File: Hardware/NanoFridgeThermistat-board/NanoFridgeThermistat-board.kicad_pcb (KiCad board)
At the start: 2 copper layers, 80.5 x 72.1 mm, 63 parts, among them J1 Connector_Thermistor, J2 Main_Connector, J3 CompressorMotor_Connector, J4 I2C_Conn, J5 Connector_Thermistor, SW1 SW_Push, SW2 SW_Push, T1 CST1, U1 MOC3042M, U2 TL072

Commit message: Added mother-daughter boards connector on mother board as well
Signed-off-by: bebenlebricolo <benoittarrade@hotmail.fr>
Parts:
- added J6: Connector_Thermistor, Connector_PinSocket_2.54mm:PinSocket_1x02_P2.54mm_Vertical, F.Cu at (120.4, 115.8)
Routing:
- net GND: track 15.5 -> 17.5 mm, vias 37 -> 36
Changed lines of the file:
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@@
     )
   )
+  (footprint "Connector_PinSocket_2.54mm:PinSocket_1x02_P2.54mm_Vertical" (layer "F.Cu")
+    (at 120.396 115.824)
+    (descr "Through hole straight socket strip, 1x02, 2.54mm pitch, single row (from Kicad 4.0.7), script generated")
+    (tags "Through hole socket strip THT 1x02 2.54mm single row")
+    (property "Sheetfile" "NanoFridgeThermistat-board.kicad_sch")
+    (property "Sheetname" "")
+    (property "ki_description" "Generic connector, single row, 01x02, script generated")
+    (property "ki_keywords" "connector")
+    (attr through_hole)
+    (fp_text reference "J6" (at -0.508 -2.794) (layer "F.SilkS")
+        (effects (font (size 1 1) (thickness 0.15)))
+    )
+    (fp_text value "Connector_Thermistor" (at 0 5.31) (layer "F.Fab")
+        (effects (font (size 1 1) (thickness 0.15)))
+    )
+    (fp_text user "${REFERENCE}" (at 0 1.27 90) (layer "F.Fab")
+        (effects (font (size 1 1) (thickness 0.15)))
+    )
+    (fp_line (start -1.33 1.27) (end -1.33 3.87)
+      (stroke (width 0.12) (type solid)) (layer "F.SilkS"))
+    (fp_line (start -1.33 1.27) (end 1.33 1.27)
+      (stroke (width 0.12) (type solid)) (layer "F.SilkS"))
+    (fp_line (start -1.33 3.87) (end 1.33 3.87)
+      (stroke (width 0.12) (type solid)) (layer "F.SilkS"))
+    (fp_line (start 0 -1.33) (end 1.33 -1.33)
+      (stroke (width 0.12) (type solid)) (layer "F.SilkS"))
+    (fp_line (start 1.33 -1.33) (end 1.33 0)
+      (stroke (width 0.12) (type solid)) (layer "F.SilkS"))
+    (fp_line (start 1.33 1.27) (end 1.33 3.87)
+      (stroke (width 0.12) (type solid)) (layer "F.SilkS"))
+    (fp_line (start -1.8 -1.8) (end 1.75 -1.8)
+      (stroke (width 0.05) (type solid)) (layer "F.CrtYd"))
+    (fp_line (start -1.8 4.3) (end -1.8 -1.8)
+      (stroke (width 0.05) (type solid)) (layer "F.CrtYd"))
+    (fp_line (start 1.75 -1.8) (end 1.75 4.3)
+      (stroke (width 0.05) (type solid)) (layer "F.CrtYd"))
+    (fp_line (start 1.75 4.3) (end -1.8 4.3)
+      (stroke (width 0.05) (type solid)) (layer "F.CrtYd"))
+    (fp_line (start -1.27 -1.27) (end 0.635 -1.27)
+      (stroke (width 0.1) (type solid)) (layer "F.Fab"))
+    (fp_line (start -1.27 3.81) (end -1.27 -1.27)
+      (stroke (width 0.1) (type solid)) (layer "F.Fab"))
+    (fp_line (start 0.635 -1.27) (end 1.27 -0.635)
+      (stroke (width 0.1) (type solid)) (layer "F.Fab"))
+    (fp_line (start 1.27 -0.635) (end 1.27 3.81)
+      (stroke (width 0.1) (type solid)) (layer "F.Fab"))
+    (fp_line (start 1.27 3.81) (end -1.27 3.81)
+      (stroke (width 0.1) (type solid)) (layer "F.Fab"))
+    (pad "1" thru_hole rect (at 0 0) (size 1.7 1.7) (drill 1) (layers "*.Cu" "*.Mask")
+      (net 21 "/TriacDriverEnable") (pinfunction "Pin_1") (pintype "passive"))
+    (pad "2" thru_hole oval (at 0 2.54) (size 1.7 1.7) (drill 1) (layers "*.Cu" "*.Mask")
+      (net 2 "GND") (pinfunction "Pin_2") (pintype "passive"))
+    (model "${KICAD6_3DMODEL_DIR}/Connector_PinSocket_2.54mm.3dshapes/PinSocket_1x02_P2.54mm_Vertical.wrl"
+      (offset (xyz 0 0 0))
+      (scale (xyz 1 1 1))
+      (rotate (xyz 0 0 0))
+    )
+  )
   (footprint "Panelization:mouse-bite-1mm-slot" (layer "F.Cu")
     (at 154.432 94.996)
@@
   (gr_line (start 134.62 95.504) (end 152.908 95.504)
     (stroke (width 0.1) (type default)) (layer "Edge.Cuts"))
-  (gr_line (start 155.956 95.536248) (end 158.496508 95.536248)
-    (stroke (width 0.1) (type default)) (layer "Edge.Cuts"))
   (gr_line (start 83.010001 131.27) (end 121.158 131.318041)
     (stroke (width 0.1) (type default)) (layer "Edge.Cuts"))
@@
   (gr_arc (start 124.206 106.426) (mid 124.714 105.918) (end 125.222 106.426)
     (stroke (width 0.1) (type default)) (layer "Edge.Cuts"))
+  (gr_line (start 155.956 95.536248) (end 158.496508 95.536248)
+    (stroke (width 0.1) (type default)) (layer "Edge.Cuts"))
   (gr_line (start 125.222 103.378) (end 125.222 97.504)
     (stroke (width 0.1) (type default)) (layer "Edge.Cuts"))
@@
     (effects (font (size 1 1) (thickness 0.15)) (justify left bottom))
   )
+  (gr_text "+" (at 121.92 116.332) (layer "F.SilkS")
+    (effects (font (size 1 1) (thickness 0.15)) (justify left bottom))
+  )
+  (gr_text "-" (at 121.92 118.872) (layer "F.SilkS")
+    (effects (font (size 1 1) (thickness 0.15)) (justify left bottom))
+  )
   (gr_text "Comp" (at 157.988 122.682 90) (layer "F.SilkS")
     (effects (font (size 1 1) (thickness 0.15)) (justify left bottom))
@@
   (segment (start 124.206 117.602) (end 125.73 117.602) (width 0.25) (layer "F.Cu") (net 2))
   (segment (start 127.508 119.126) (end 126.873 119.126) (width 0.25) (layer "F.Cu") (net 2))
-  (segment (start 121.412 117.602) (end 124.206 117.602) (width 0.25) (layer "F.Cu") (net 2))
   (segment (start 131.846 112.731) (end 130.048 114.529) (width 0.25) (layer "F.Cu") (net 2))
+  (segment (start 120.396 118.364) (end 121.158 117.602) (width 0.25) (layer "F.Cu") (net 2))
   (segment (start 130.048 114.529) (end 130.048 116.586) (width 0.25) (layer "F.Cu") (net 2))
   (segment (start 125.73 117.602) (end 126.873 118.745) (width 0.25) (layer "F.Cu") (net 2))
   (segment (start 126.873 118.745) (end 126.873 119.126) (width 0.25) (layer "F.Cu") (net 2))
   (segment (start 130.048 116.586) (end 127.508 119.126) (width 0.25) (layer "F.Cu") (net 2))
-  (segment (start 121.158 117.348) (end 121.412 117.602) (width 0.25) (layer "F.Cu") (net 2))
+  (segment (start 121.158 117.602) (end 125.222 117.602) (width 0.25) (layer "F.Cu") (net 2))
   (via (at 112.776 104.14) (size 0.8) (drill 0.4) (layers "F.Cu" "B.Cu") (free) (net 2))
   (via (at 91.948 70.104) (size 0.8) (drill 0.4) (layers "F.Cu" "B.Cu") (free) (net 2))
   (via (at 99.568 105.664) (size 0.8) (drill 0.4) (layers "F.Cu" "B.Cu") (free) (net 2))
-  (via (at 121.158 117.348) (size 0.8) (drill 0.4) (layers "F.Cu" "B.Cu") (free) (net 2))
   (via (at 87.376 67.056) (size 0.8) (drill 0.4) (layers "F.Cu" "B.Cu") (free) (net 2))
   (via (at 91.44 99.06) (size 0.8) (drill 0.4) (layers "F.Cu" "B.Cu") (free) (net 2))

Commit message: Added Open Source Hardware logo to boards
Signed-off-by: bebenlebricolo <benoittarrade@hotmail.fr>
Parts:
- added REF**: OSHW-Logo2_7.3x6mm_SilkScreen, Symbol:OSHW-Logo2_7.3x6mm_SilkScreen, B.Cu at (142.0, 119.4)
- added REF**: OSHW-Logo2_9.8x8mm_SilkScreen, Symbol:OSHW-Logo2_9.8x8mm_SilkScreen, B.Cu at (102.1, 113.3)

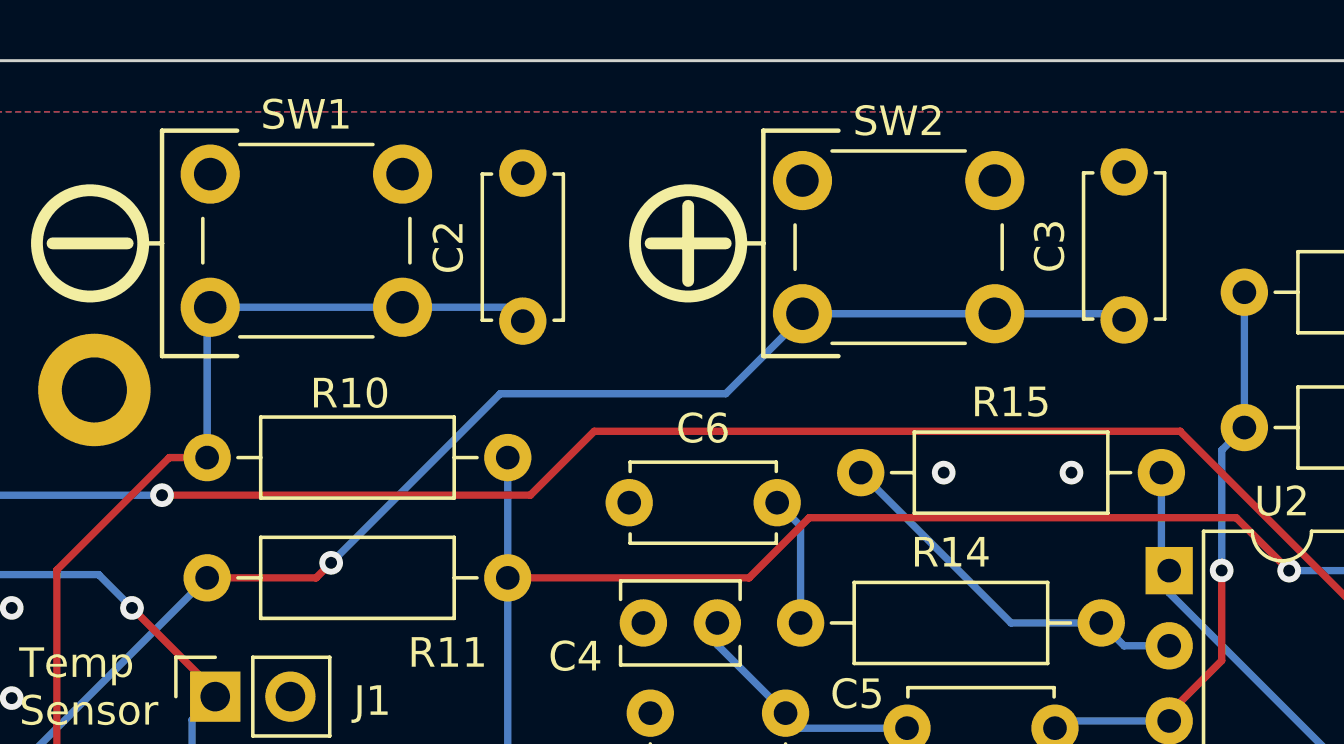
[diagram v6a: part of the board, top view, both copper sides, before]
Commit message: harware : swapped misplaced buttons
Signed-off-by: bebenlebricolo <benoittarrade@hotmail.fr>
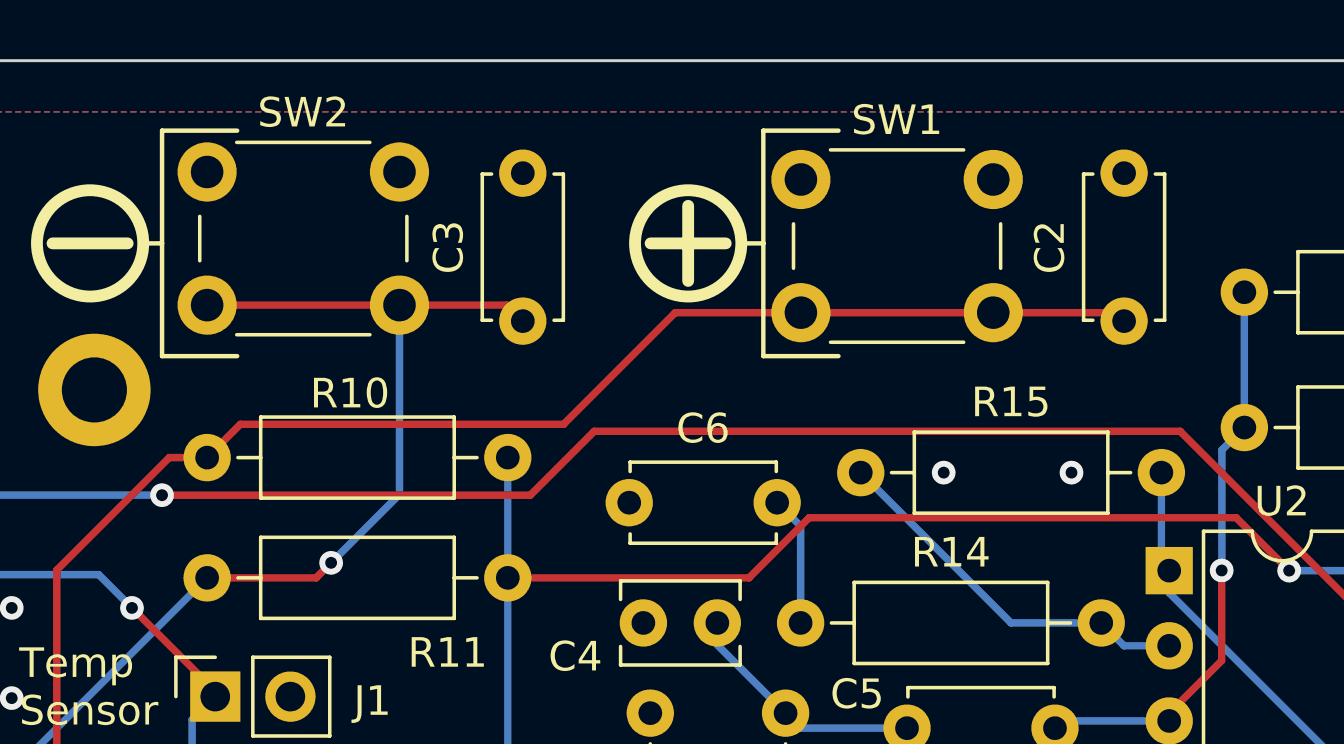
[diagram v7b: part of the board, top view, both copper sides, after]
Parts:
- moved C3 20.3 mm to (118.9, 68.0)
- moved C2 20.3 mm to (139.2, 68.0)
- moved SW2 20.1 mm to (108.2, 63.0)
- moved SW1 20.0 mm to (128.3, 63.2)
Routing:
- net +Button: track 59.4 -> 76.6 mm
- net -Button: track 76.9 -> 67.1 mm
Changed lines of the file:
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@@
   )
   (footprint "Capacitor_THT:C_Disc_D4.7mm_W2.5mm_P5.00mm" (layer "F.Cu")
-    (at 118.872 68.032 90)
+    (at 139.192 68.032 90)
     (descr "C, Disc series, Radial, pin pitch=5.00mm, , diameter*width=4.7*2.5mm^2, Capacitor, http://www.vishay.com/docs/45233/krseries.pdf")
     (tags "C Disc series Radial pin pitch 5.00mm  diameter 4.7mm width 2.5mm Capacitor")
@@
   )
   (footprint "Button_Switch_THT:SW_PUSH_6mm" (layer "F.Cu")
-    (at 128.322 63.282)
+    (at 108.204 62.992)
     (descr "https://www.omron.com/ecb/products/pdf/en-b3f.pdf")
     (tags "tact sw push 6mm")
@@
   )
   (footprint "Capacitor_THT:C_Disc_D4.7mm_W2.5mm_P5.00mm" (layer "F.Cu")
-    (at 139.192 67.992 90)
+    (at 118.872 68.032 90)
     (descr "C, Disc series, Radial, pin pitch=5.00mm, , diameter*width=4.7*2.5mm^2, Capacitor, http://www.vishay.com/docs/45233/krseries.pdf")
     (tags "C Disc series Radial pin pitch 5.00mm  diameter 4.7mm width 2.5mm Capacitor")
@@
   )
   (footprint "Button_Switch_THT:SW_PUSH_6mm" (layer "F.Cu")
-    (at 108.308 63.064)
+    (at 128.27 63.246)
     (descr "https://www.omron.com/ecb/products/pdf/en-b3f.pdf")
     (tags "tact sw push 6mm")
@@
   (segment (start 98.298 91.694) (end 100.744495 91.694) (width 0.25) (layer "F.Cu") (net 33))
   (segment (start 97.028 90.424) (end 98.298 91.694) (width 0.25) (layer "F.Cu") (net 33))
+  (segment (start 108.204 72.644) (end 109.329 71.519) (width 0.25) (layer "F.Cu") (net 33))
+  (segment (start 120.251 71.519) (end 124.024 67.746) (width 0.25) (layer "F.Cu") (net 33))
   (segment (start 106.426 97.375505) (end 106.426 105.41) (width 0.25) (layer "F.Cu") (net 33))
+  (segment (start 109.329 71.519) (end 120.251 71.519) (width 0.25) (layer "F.Cu") (net 33))
+  (segment (start 138.906 67.746) (end 139.192 68.032) (width 0.25) (layer "F.Cu") (net 33))
   (segment (start 106.924695 72.644) (end 103.124 76.444695) (width 0.25) (layer "F.Cu") (net 33))
   (segment (start 108.204 72.644) (end 106.924695 72.644) (width 0.25) (layer "F.Cu") (net 33))
   (segment (start 103.124 84.328) (end 99.568 87.884) (width 0.25) (layer "F.Cu") (net 33))
+  (segment (start 128.27 67.746) (end 134.77 67.746) (width 0.25) (layer "F.Cu") (net 33))
   (segment (start 100.744495 91.694) (end 106.426 97.375505) (width 0.25) (layer "F.Cu") (net 33))
   (segment (start 103.124 76.444695) (end 103.124 84.328) (width 0.25) (layer "F.Cu") (net 33))
+  (segment (start 134.77 67.746) (end 138.906 67.746) (width 0.25) (layer "F.Cu") (net 33))
+  (segment (start 124.024 67.746) (end 128.27 67.746) (width 0.25) (layer "F.Cu") (net 33))
   (via (at 97.028 90.424) (size 0.8) (drill 0.4) (layers "F.Cu" "B.Cu") (net 33))
-  (segment (start 108.204 67.668) (end 108.308 67.564) (width 0.25) (layer "B.Cu") (net 33))
-  (segment (start 118.404 67.564) (end 118.872 68.032) (width 0.25) (layer "B.Cu") (net 33))
-  (segment (start 108.308 67.564) (end 118.404 67.564) (width 0.25) (layer "B.Cu") (net 33))
   (segment (start 97.028 90.424) (end 99.568 87.884) (width 0.25) (layer "B.Cu") (net 33))
-  (segment (start 108.204 72.644) (end 108.204 67.668) (width 0.25) (layer "B.Cu") (net 33))
   (segment (start 104.14 105.41) (end 104.14 101.336695) (width 0.25) (layer "F.Cu") (net 34))
   (segment (start 98.697 99.459) (end 94.488 95.25) (width 0.25) (layer "F.Cu") (net 34))
@@
   (segment (start 94.488 95.25) (end 94.488 87.63) (width 0.25) (layer "F.Cu") (net 34))
   (segment (start 102.262305 99.459) (end 98.697 99.459) (width 0.25) (layer "F.Cu") (net 34))
+  (segment (start 114.704 67.492) (end 118.332 67.492) (width 0.25) (layer "F.Cu") (net 34))
   (segment (start 111.887 76.708) (end 108.204 76.708) (width 0.25) (layer "F.Cu") (net 34))
+  (segment (start 108.204 67.492) (end 114.704 67.492) (width 0.25) (layer "F.Cu") (net 34))
+  (segment (start 118.332 67.492) (end 118.872 68.032) (width 0.25) (layer "F.Cu") (net 34))
   (segment (start 104.14 101.336695) (end 102.262305 99.459) (width 0.25) (layer "F.Cu") (net 34))
   (via (at 112.395 76.2) (size 0.8) (drill 0.4) (layers "F.Cu" "B.Cu") (net 34))
   (via (at 94.488 87.63) (size 0.8) (drill 0.4) (layers "F.Cu" "B.Cu") (net 34))
-  (segment (start 128.322 67.893) (end 128.322 67.782) (width 0.25) (layer "B.Cu") (net 34))
   (segment (start 94.488 87.63) (end 96.774 85.344) (width 0.25) (layer "B.Cu") (net 34))
-  (segment (start 112.395 76.2) (end 118.11 70.485) (width 0.25) (layer "B.Cu") (net 34))
-  (segment (start 125.73 70.485) (end 128.322 67.893) (width 0.25) (layer "B.Cu") (net 34))
-  (segment (start 128.322 67.782) (end 138.982 67.782) (width 0.25) (layer "B.Cu") (net 34))
-  (segment (start 138.982 67.782) (end 139.192 67.992) (width 0.25) (layer "B.Cu") (net 34))
-  (segment (start 118.11 70.485) (end 125.73 70.485) (width 0.25) (layer "B.Cu") (net 34))
+  (segment (start 114.704 73.891) (end 112.395 76.2) (width 0.25) (layer "B.Cu") (net 34))
+  (segment (start 114.704 67.492) (end 114.704 73.891) (width 0.25) (layer "B.Cu") (net 34))
   (segment (start 96.774 85.344) (end 99.568 85.344) (width 0.25) (layer "B.Cu") (net 34))
   (segment (start 108.204 76.708) (end 99.568 85.344) (width 0.25) (layer "B.Cu") (net 34))
